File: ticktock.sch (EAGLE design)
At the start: 59 parts, among them IC1 ATMEGA644A, IC2 AD8611R, IC3 REF200U, J1 AVR_SPI_PRG_6NS, Q1 MOSFET-NCHANNEL2N7002PW, Q2 MOSFET-NCHANNELBSS138, Q3 MOSFET-NCHANNELBSS138, U1 MAX232SOIC16, U2 OSCILLATORSMD, U3 FT232RLSSOP, U4 BMP180

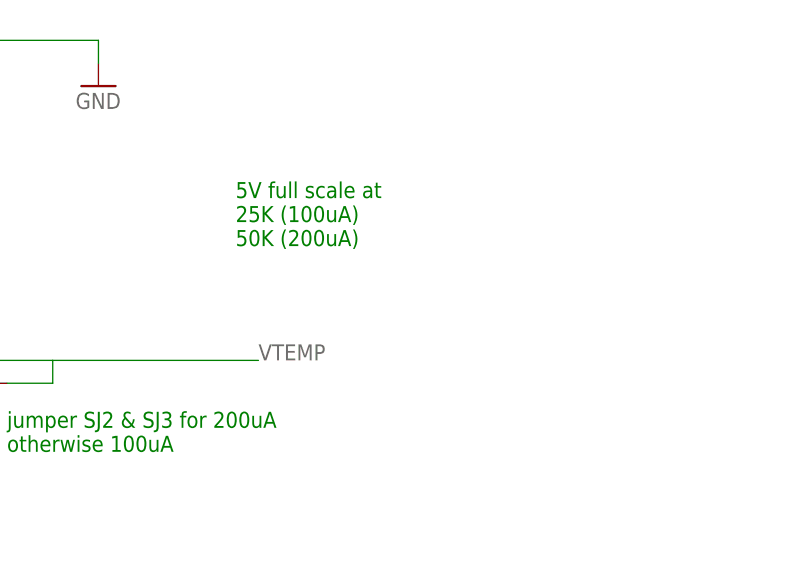
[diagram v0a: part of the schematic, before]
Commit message: Add thermistor info in a label
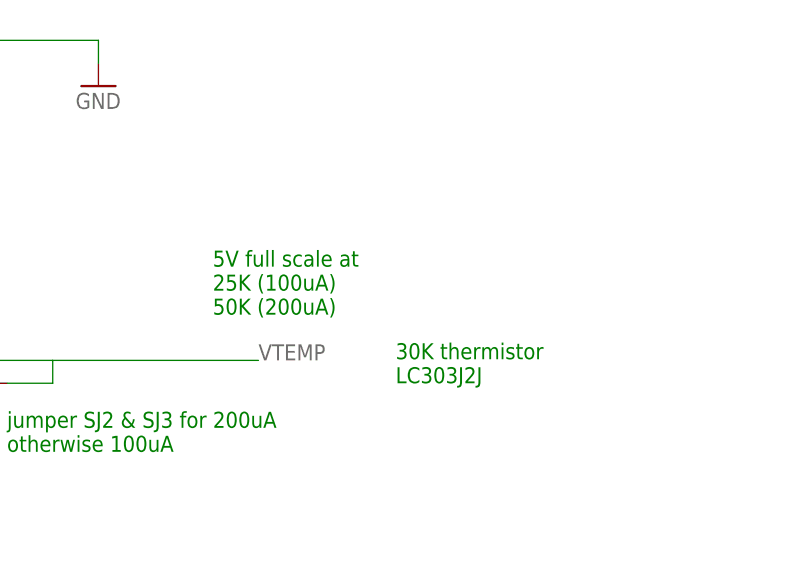
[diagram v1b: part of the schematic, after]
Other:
- note added: "30K thermistor LC303J2J"
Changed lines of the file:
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@@
 <text x="411.48" y="60.96" size="1.778" layer="91">jumper SJ2 &amp; SJ3 for 200uA
 otherwise 100uA</text>
-<text x="436.88" y="83.82" size="1.778" layer="91">5V full scale at
+<text x="434.34" y="76.2" size="1.778" layer="91">5V full scale at
 25K (100uA)
 50K (200uA)</text>
+<text x="454.66" y="68.58" size="1.778" layer="91">30K thermistor
+LC303J2J</text>
 </plain>
 <instances>

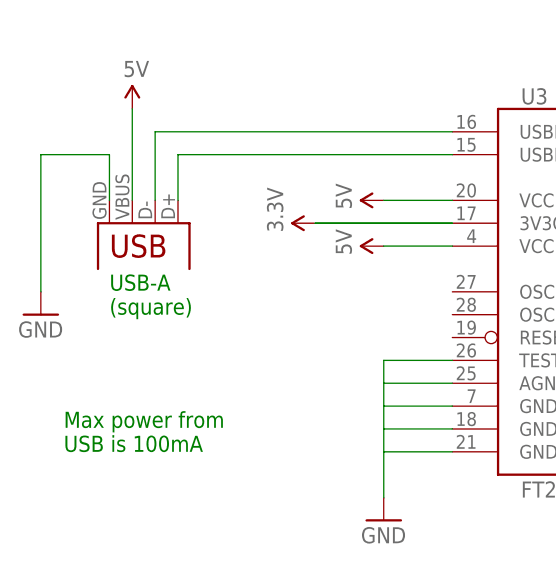
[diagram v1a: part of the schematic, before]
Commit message: Fix USB connector label (A -> B)
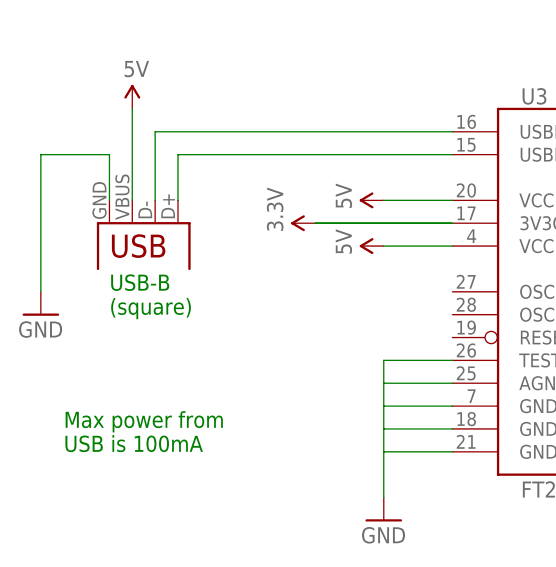
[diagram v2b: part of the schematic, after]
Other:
- note added: "USB-B (square)"
- note removed: "USB-A (square)"
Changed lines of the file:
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@@
 TX =&gt; RX(2), TX(3) =&gt; RX
 </text>
-<text x="20.32" y="40.64" size="1.778" layer="91">USB-A
+<text x="20.32" y="40.64" size="1.778" layer="91">USB-B
 (square)</text>
 <text x="15.24" y="25.4" size="1.778" layer="91">Max power from

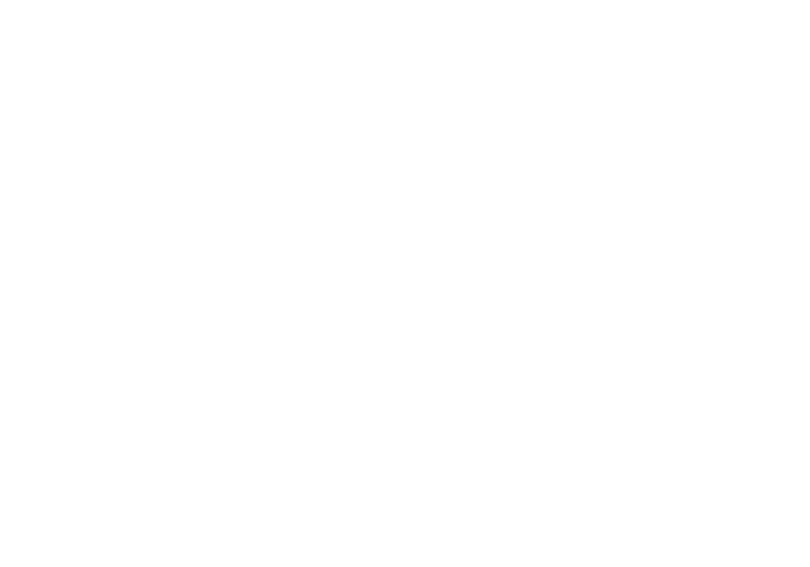
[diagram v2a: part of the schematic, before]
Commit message: Replace existing holes with SparkFun #4 standoff holes
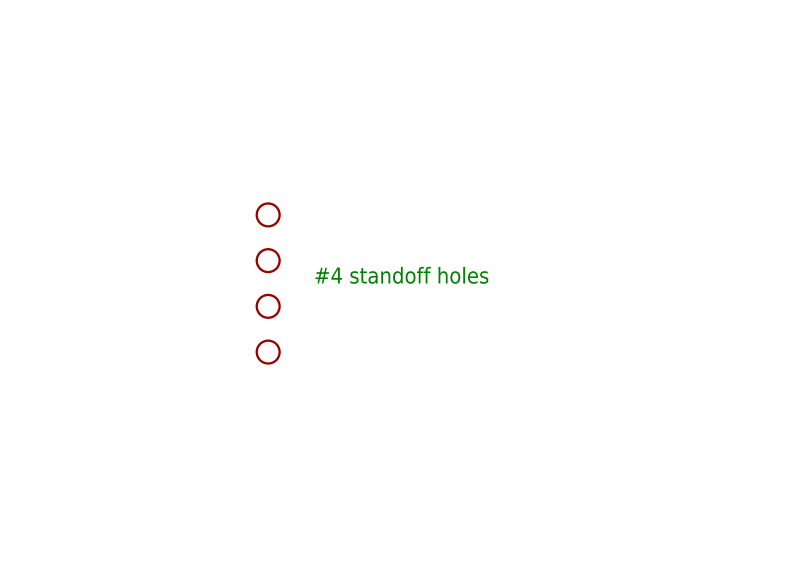
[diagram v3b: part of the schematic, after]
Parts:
- added STANDOFF1, STANDOFF2, STANDOFF3, STANDOFF4: STAND-OFF, SparkFun-Electromechanical:STAND-OFF
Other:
- note added: "#4 standoff holes"
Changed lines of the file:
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@@
 <part name="SUPPLY31" library="SparkFun-Aesthetics" deviceset="5V" device=""/>
 <part name="GND25" library="SparkFun-Aesthetics" deviceset="GND" device=""/>
+<part name="STANDOFF1" library="SparkFun-Electromechanical" deviceset="STAND-OFF" device=""/>
+<part name="STANDOFF2" library="SparkFun-Electromechanical" deviceset="STAND-OFF" device=""/>
+<part name="STANDOFF3" library="SparkFun-Electromechanical" deviceset="STAND-OFF" device=""/>
+<part name="STANDOFF4" library="SparkFun-Electromechanical" deviceset="STAND-OFF" device=""/>
 </parts>
 <sheets>
@@
 <text x="454.66" y="68.58" size="1.778" layer="91">30K thermistor
 LC303J2J</text>
+<text x="492.76" y="299.72" size="1.778" layer="91">#4 standoff holes</text>
 </plain>
 <instances>
@@
 <instance part="SUPPLY31" gate="G$1" x="421.64" y="124.46"/>
 <instance part="GND25" gate="1" x="421.64" y="101.6"/>
+<instance part="STANDOFF1" gate="G$1" x="487.68" y="307.34"/>
+<instance part="STANDOFF2" gate="G$1" x="487.68" y="302.26"/>
+<instance part="STANDOFF3" gate="G$1" x="487.68" y="297.18"/>
+<instance part="STANDOFF4" gate="G$1" x="487.68" y="292.1"/>
 </instances>
 <busses>

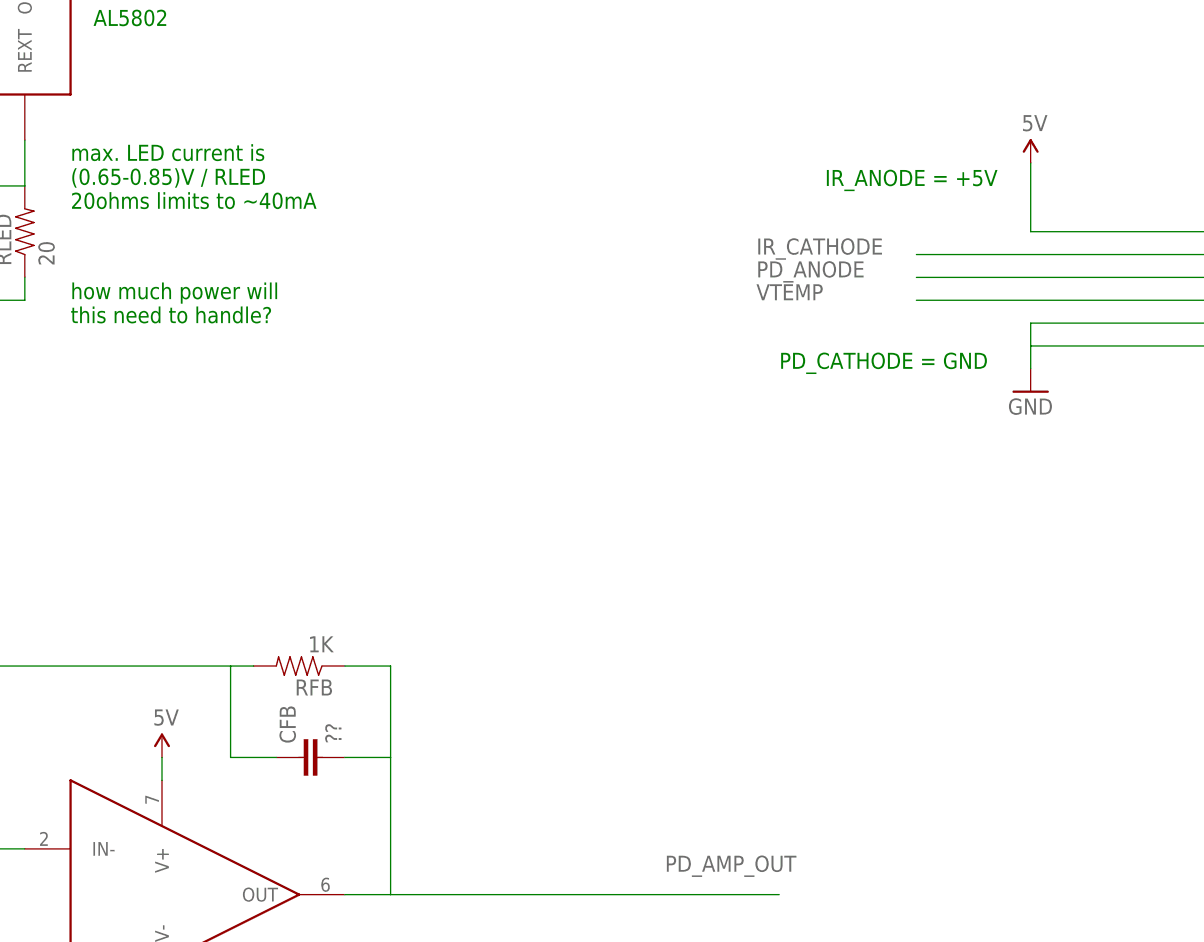
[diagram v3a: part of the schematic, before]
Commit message: fix schematic broken connections
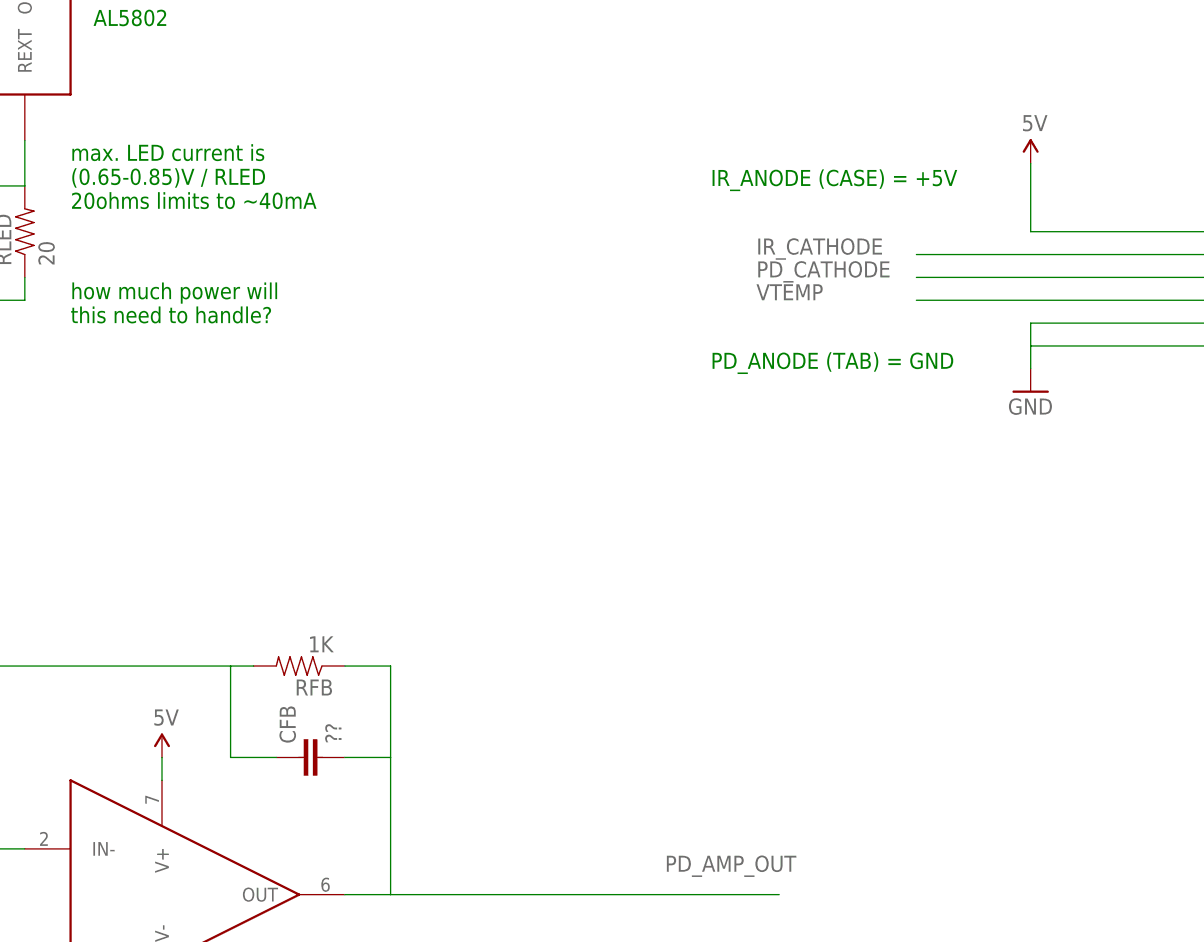
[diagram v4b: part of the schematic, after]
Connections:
- removed net N$22: D1.C
- removed net PD_ANODE: PKG-CABLE.3
- net 5V: now also U$1.V+
- net PD_AMP_OUT: now also U$1.OUT
- net PD_CATHODE: now also PKG-CABLE.3
- net RED_LED: now also D1.C
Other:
- note added: "IR_ANODE (CASE) = +5V"
- note added: "PD_ANODE (TAB) = GND"
- note removed: "IR_ANODE = +5V"
- note removed: "PD_CATHODE = GND"
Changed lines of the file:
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@@
 <text x="86.36" y="129.54" size="1.778" layer="91">See Fig 23-9 on
 p.254 of datasheet</text>
-<text x="182.88" y="360.68" size="1.778" layer="91">IR_ANODE = +5V</text>
+<text x="170.18" y="360.68" size="1.778" layer="91">IR_ANODE (CASE) = +5V</text>
 <text x="88.9" y="162.56" size="1.778" layer="91">XTAL2 is NC
 See Fig 9-4</text>
@@
 TAB = anode = IN+ (GND)
 CASE = cathode = IN-</text>
-<text x="177.8" y="340.36" size="1.778" layer="91">PD_CATHODE = GND</text>
+<text x="170.18" y="340.36" size="1.778" layer="91">PD_ANODE (TAB) = GND</text>
 <text x="363.22" y="48.26" size="1.778" layer="91">jumper for best DC performance
 leave open for best AC performance</text>
@@
 </segment>
 <segment>
-<pinref part="SUPPLY17" gate="G$1" pin="5V"/>
-<wire x1="109.22" y1="297.18" x2="109.22" y2="294.64" width="0.1524" layer="91"/>
-</segment>
-<segment>
 <pinref part="SUPPLY18" gate="G$1" pin="5V"/>
 <wire x1="96.52" y1="251.46" x2="96.52" y2="248.92" width="0.1524" layer="91"/>
@@
 <pinref part="SUPPLY31" gate="G$1" pin="5V"/>
 <wire x1="421.64" y1="121.92" x2="421.64" y2="124.46" width="0.1524" layer="91"/>
+</segment>
+<segment>
+<pinref part="U$1" gate="G$1" pin="V+"/>
+<pinref part="SUPPLY17" gate="G$1" pin="5V"/>
+<wire x1="109.22" y1="294.64" x2="109.22" y2="297.18" width="0.1524" layer="91"/>
 </segment>
 </net>
@@
 <net name="PD_AMP_OUT" class="0">
 <segment>
-<wire x1="129.54" y1="281.94" x2="134.62" y2="281.94" width="0.1524" layer="91"/>
 <label x="165.1" y="284.48" size="1.778" layer="95"/>
 <pinref part="RFB" gate="G$1" pin="1"/>
@@
 <wire x1="129.54" y1="297.18" x2="134.62" y2="297.18" width="0.1524" layer="91"/>
 <wire x1="134.62" y1="297.18" x2="134.62" y2="281.94" width="0.1524" layer="91"/>
+<pinref part="U$1" gate="G$1" pin="OUT"/>
+<wire x1="129.54" y1="281.94" x2="134.62" y2="281.94" width="0.1524" layer="91"/>
 </segment>
 <segment>
@@
 <label x="53.34" y="289.56" size="1.778" layer="95"/>
 </segment>
-</net>
-<net name="PD_ANODE" class="0">
 <segment>
 <pinref part="PKG-CABLE" gate="G$1" pin="3"/>
@@
 </segment>
 </net>
-<net name="N$22" class="0">
-<segment>
-<pinref part="D1" gate="G$1" pin="C"/>
-<wire x1="238.76" y1="147.32" x2="238.76" y2="139.7" width="0.1524" layer="91"/>
-</segment>
-</net>
 <net name="YELLOW_LED" class="0">
 <segment>
@@
 <wire x1="165.1" y1="139.7" x2="238.76" y2="139.7" width="0.1524" layer="91"/>
 <label x="226.06" y="139.7" size="1.778" layer="95"/>
-</segment>
-</net>
+<pinref part="D1" gate="G$1" pin="C"/>
+<wire x1="238.76" y1="147.32" x2="238.76" y2="139.7" width="0.1524" layer="91"/>
+</segment>
+</net>

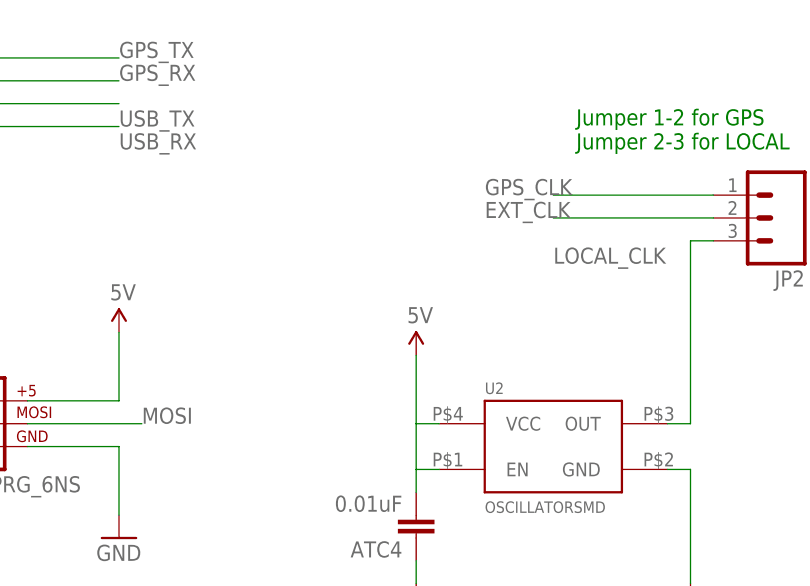
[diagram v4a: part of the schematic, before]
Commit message: Add power jumper for local 10MHz
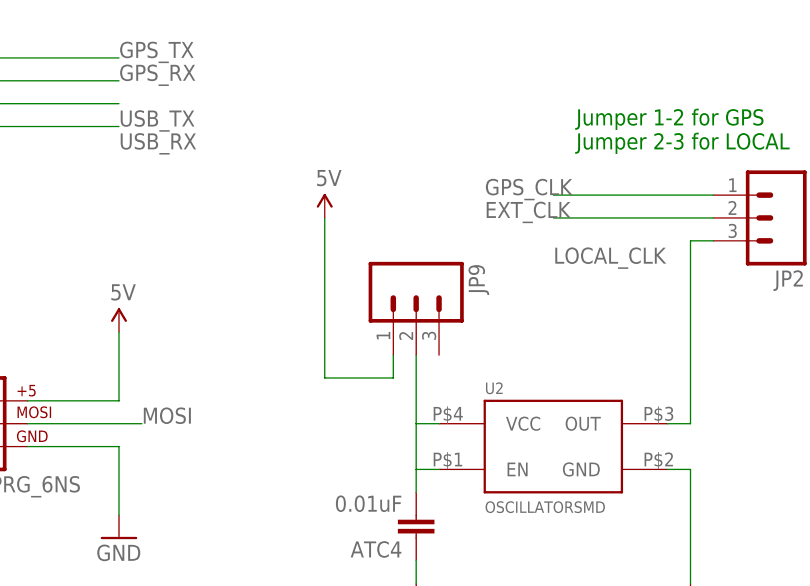
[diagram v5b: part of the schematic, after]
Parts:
- added JP9: (no value), SparkFun-Connectors:M03LOCK
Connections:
- new net N$22: ATC4.2, JP9.2, U2.EN, U2.VCC
- net 5V: now also JP9.1; no longer ATC4.2, U2.EN, U2.VCC
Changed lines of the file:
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@@
 <part name="STANDOFF3" library="SparkFun-Electromechanical" deviceset="STAND-OFF" device=""/>
 <part name="STANDOFF4" library="SparkFun-Electromechanical" deviceset="STAND-OFF" device=""/>
+<part name="JP9" library="SparkFun-Connectors" deviceset="M03" device="LOCK"/>
 </parts>
 <sheets>
@@
 <instance part="GND14" gate="1" x="187.96" y="55.88"/>
 <instance part="U2" gate="G$1" x="236.22" y="66.04"/>
-<instance part="SUPPLY15" gate="G$1" x="220.98" y="76.2"/>
+<instance part="SUPPLY15" gate="G$1" x="210.82" y="91.44"/>
 <instance part="GND15" gate="1" x="251.46" y="48.26"/>
 <instance part="GND16" gate="1" x="220.98" y="48.26"/>
@@
 <instance part="STANDOFF3" gate="G$1" x="487.68" y="297.18"/>
 <instance part="STANDOFF4" gate="G$1" x="487.68" y="292.1"/>
+<instance part="JP9" gate="G$1" x="220.98" y="83.82" rot="R270"/>
 </instances>
 <busses>
@@
 </segment>
 <segment>
-<pinref part="SUPPLY15" gate="G$1" pin="5V"/>
-<wire x1="220.98" y1="76.2" x2="220.98" y2="68.58" width="0.1524" layer="91"/>
-<pinref part="U2" gate="G$1" pin="EN"/>
-<wire x1="220.98" y1="68.58" x2="220.98" y2="63.5" width="0.1524" layer="91"/>
-<wire x1="220.98" y1="63.5" x2="223.52" y2="63.5" width="0.1524" layer="91"/>
-<pinref part="U2" gate="G$1" pin="VCC"/>
-<wire x1="223.52" y1="68.58" x2="220.98" y2="68.58" width="0.1524" layer="91"/>
-<pinref part="ATC4" gate="G$1" pin="2"/>
-<wire x1="220.98" y1="63.5" x2="220.98" y2="60.96" width="0.1524" layer="91"/>
-</segment>
-<segment>
 <pinref part="IC2" gate="G$1" pin="V+"/>
 <pinref part="SUPPLY16" gate="G$1" pin="5V"/>
@@
 <pinref part="SUPPLY17" gate="G$1" pin="5V"/>
 <wire x1="109.22" y1="294.64" x2="109.22" y2="297.18" width="0.1524" layer="91"/>
+</segment>
+<segment>
+<pinref part="JP9" gate="G$1" pin="1"/>
+<wire x1="218.44" y1="76.2" x2="218.44" y2="73.66" width="0.1524" layer="91"/>
+<wire x1="218.44" y1="73.66" x2="210.82" y2="73.66" width="0.1524" layer="91"/>
+<pinref part="SUPPLY15" gate="G$1" pin="5V"/>
+<wire x1="210.82" y1="73.66" x2="210.82" y2="91.44" width="0.1524" layer="91"/>
 </segment>
 </net>
@@
 </segment>
 </net>
+<net name="N$22" class="0">
+<segment>
+<pinref part="U2" gate="G$1" pin="EN"/>
+<wire x1="220.98" y1="68.58" x2="220.98" y2="63.5" width="0.1524" layer="91"/>
+<wire x1="220.98" y1="63.5" x2="223.52" y2="63.5" width="0.1524" layer="91"/>
+<pinref part="U2" gate="G$1" pin="VCC"/>
+<wire x1="223.52" y1="68.58" x2="220.98" y2="68.58" width="0.1524" layer="91"/>
+<pinref part="ATC4" gate="G$1" pin="2"/>
+<wire x1="220.98" y1="63.5" x2="220.98" y2="60.96" width="0.1524" layer="91"/>
+<pinref part="JP9" gate="G$1" pin="2"/>
+<wire x1="220.98" y1="68.58" x2="220.98" y2="76.2" width="0.1524" layer="91"/>
+</segment>
+</net>
